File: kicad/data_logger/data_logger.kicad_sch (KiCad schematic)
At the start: 14 parts, among them M2 Motor_DC, M3 Motor_DC, M4 Motor_DC, U1 ARDUINO_MKR_WAN_1310

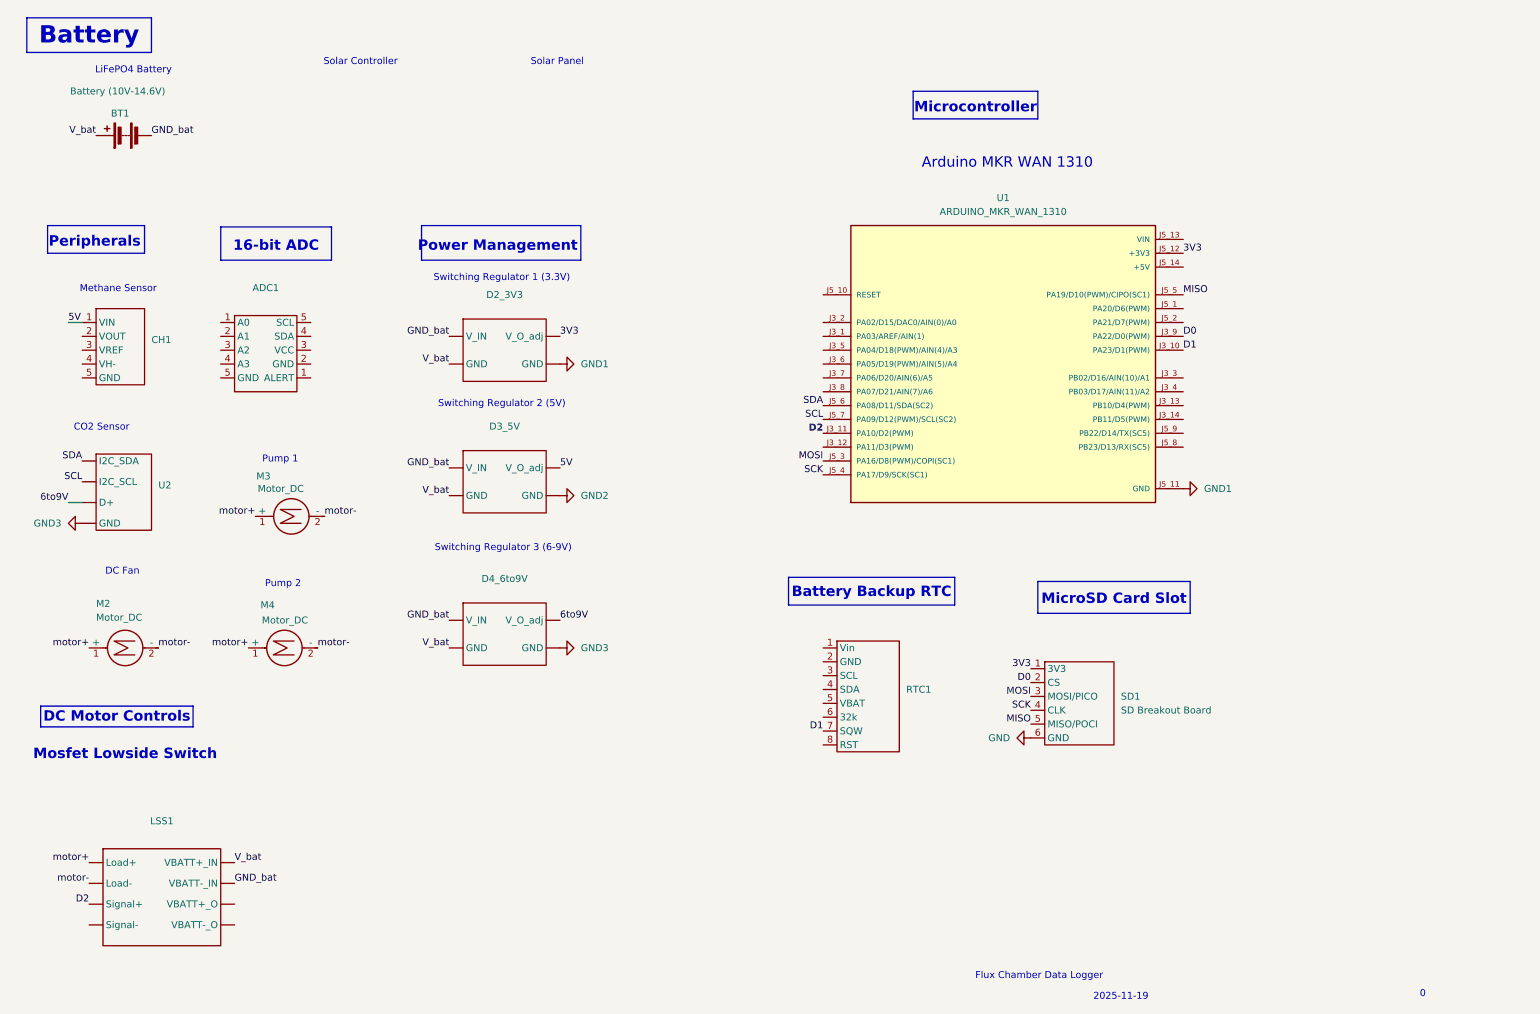
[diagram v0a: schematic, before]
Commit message: Updating schematics as I resolder things to the prototype
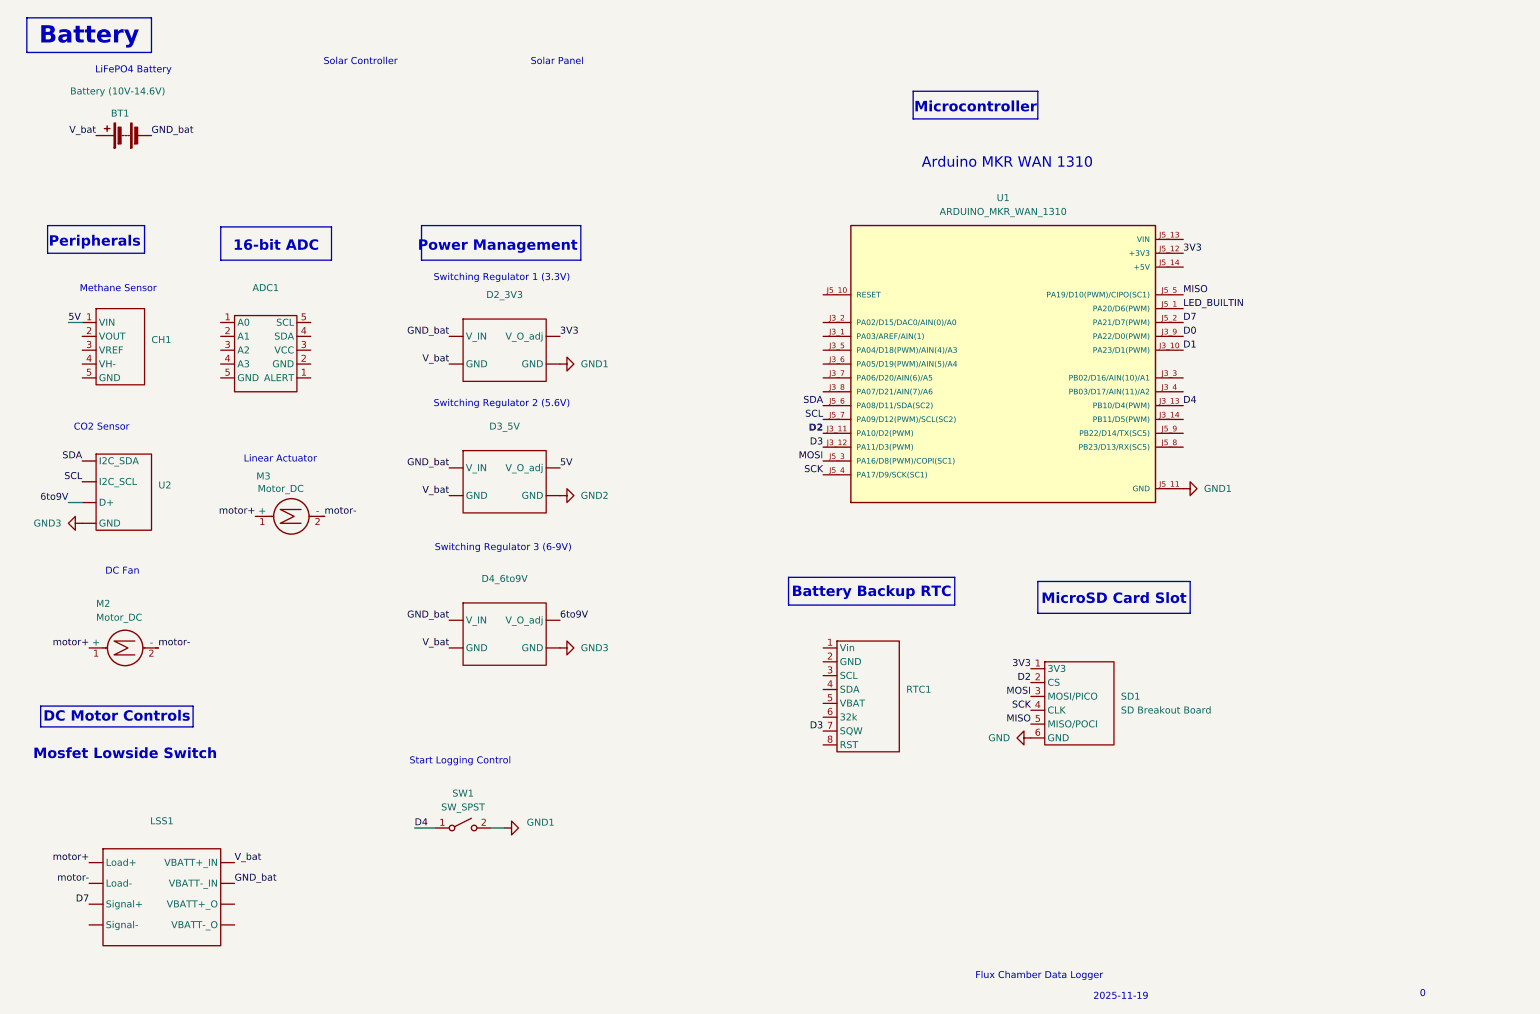
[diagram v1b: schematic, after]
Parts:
- removed M4: Motor_DC, symbol Motor:Motor_DC
- added SW1: SW_SPST, symbol Switch:SW_SPST
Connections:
- net D0: no longer SD1.2 (CS)
- net D1: no longer RTC1.7 (SQW)
- net D2: now also SD1.2 (CS); no longer LSS1. (VBATT-_O)
- net GND1: now also SW1.2 (B)
- net D3: now reaches U1.J3_12 (PA11/D3(PWM))
- net D3: now also RTC1.7 (SQW)
- net D4: now reaches U1.J3_13 (PB10/D4(PWM))
- net D4: now also SW1.1 (A)
- net LED_BUILTIN: now reaches U1.J5_1 (PA20/D6(PWM))
- net D7: now reaches U1.J5_2 (PA21/D7(PWM))
- net D7: now also LSS1. (VBATT-_O)
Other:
- note added: "Linear Actuator"
- note added: "Start Logging Control"
- note added: "Switching Regulator 2 (5.6V)"
- note removed: "Pump 1"
- note removed: "Pump 2"
- note removed: "Switching Regulator 2 (5V)"
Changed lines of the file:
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@@
 		)
 	)
-	(text "Pump 1"
+	(text "Linear Actuator\n"
 		(exclude_from_sim no)
 		(at 60.452 94.996 0)
@@
 		)
 	)
-	(text "Switching Regulator 2 (5V)\n"
+	(text "Switching Regulator 2 (5.6V)\n"
 		(exclude_from_sim no)
 		(at 101.092 84.836 0)
@@
 		)
 	)
-	(text "Pump 2"
-		(exclude_from_sim no)
-		(at 60.96 117.856 0)
+	(text "Start Logging Control"
+		(exclude_from_sim no)
+		(at 93.472 150.368 0)
 		(effects
 			(font
@@
 	(wire
 		(pts
-			(xy 21.59 69.85) (xy 24.13 69.85)
+			(xy 88.9 162.56) (xy 85.09 162.56)
 		)
 		(stroke
@@
 		)
 	)
+	(wire
+		(pts
+			(xy 21.59 69.85) (xy 24.13 69.85)
+		)
+		(stroke
+			(width 0)
+			(type default)
+		)
+	)
+	(wire
+		(pts
+			(xy 101.6 162.56) (xy 99.06 162.56)
+		)
+		(stroke
+			(width 0)
+			(type default)
+		)
+	)
 	(label "V_bat"
 		(at 52.07 168.91 0)
@@
 		)
 	)
-	(label "motor+"
-		(at 54.61 129.54 180)
-		(effects
-			(font
-				(size 1.27 1.27)
-			)
-			(justify right bottom)
-		)
-	)
 	(label "SDA"
 		(at 24.13 95.25 180)
@@
 		)
 	)
+	(label "D7"
+		(at 25.4 176.53 180)
+		(effects
+			(font
+				(size 1.27 1.27)
+			)
+			(justify right bottom)
+		)
+	)
 	(label "MISO"
 		(at 226.06 64.77 0)
@@
 		)
 	)
-	(label "D2"
-		(at 25.4 176.53 180)
-		(effects
-			(font
-				(size 1.27 1.27)
-			)
-			(justify right bottom)
+	(label "D4"
+		(at 226.06 85.09 0)
+		(effects
+			(font
+				(size 1.27 1.27)
+			)
+			(justify left bottom)
 		)
 	)
@@
 		)
 	)
-	(label "motor-"
-		(at 67.31 129.54 0)
-		(effects
-			(font
-				(size 1.27 1.27)
-			)
-			(justify left bottom)
-		)
-	)
 	(label "SCL"
 		(at 24.13 99.06 180)
@@
 		)
 	)
+	(label "LED_BUILTIN"
+		(at 226.06 67.31 0)
+		(effects
+			(font
+				(size 1.27 1.27)
+			)
+			(justify left bottom)
+		)
+	)
 	(label "V_bat"
 		(at 91.44 101.6 180)
@@
 		)
 	)
-	(label "D0"
+	(label "D7"
+		(at 226.06 69.85 0)
+		(effects
+			(font
+				(size 1.27 1.27)
+			)
+			(justify left bottom)
+		)
+	)
+	(label "D2"
 		(at 198.12 135.89 180)
 		(effects
@@
 		)
 	)
-	(label "D1"
+	(label "D3"
 		(at 160.02 144.78 180)
 		(effects
@@
 		)
 	)
+	(label "D4"
+		(at 85.09 162.56 0)
+		(effects
+			(font
+				(size 1.27 1.27)
+			)
+			(justify left bottom)
+		)
+	)
 	(label "V_bat"
 		(at 91.44 77.47 180)
@@
 	(label "GND_bat"
 		(at 91.44 96.52 180)
+		(effects
+			(font
+				(size 1.27 1.27)
+			)
+			(justify right bottom)
+		)
+	)
+	(label "D3"
+		(at 160.02 92.71 180)
 		(effects
 			(font
@@
 	)
 	(symbol
+		(lib_id "Switch:SW_SPST")
+		(at 93.98 162.56 0)
+		(unit 1)
+		(exclude_from_sim no)
+		(in_bom yes)
+		(on_board yes)
+		(dnp no)
+		(fields_autoplaced yes)
+		(property "Reference" "SW1"
+			(at 93.98 156.21 0)
+			(effects
+				(font
+					(size 1.27 1.27)
+				)
+			)
+		)
+		(property "Value" "SW_SPST"
+			(at 93.98 158.75 0)
+			(effects
+				(font
+					(size 1.27 1.27)
+				)
+			)
+		)
+		(property "Footprint" ""
+			(at 93.98 162.56 0)
+			(effects
+				(font
+					(size 1.27 1.27)
+				)
+				(hide yes)
+			)
+		)
+		(property "Datasheet" "~"
+			(at 93.98 162.56 0)
+			(effects
+				(font
+					(size 1.27 1.27)
+				)
+				(hide yes)
+			)
+		)
+		(property "Description" "Single Pole Single Throw (SPST) switch"
+			(at 93.98 162.56 0)
+			(effects
+				(font
+					(size 1.27 1.27)
+				)
+				(hide yes)
+			)
+		)
+		(pin "2"
+		)
+		(pin "1"
+		)
+		(instances
+			(project ""
+				(path "/6e8062db-1165-40d3-b0a8-95f723efc855"
+					(reference "SW1")
+					(unit 1)
+				)
+			)
+		)
+	)
+	(symbol
 		(lib_id "Device:Battery")
 		(at 31.75 35.56 90)
@@
 	)
 	(symbol
-		(lib_id "Motor:Motor_DC")
-		(at 59.69 129.54 90)
-		(unit 1)
-		(exclude_from_sim no)
-		(in_bom yes)
-		(on_board yes)
-		(dnp no)
-		(property "Reference" "M4"
-			(at 59.436 121.666 90)
-			(effects
-				(font
-					(size 1.27 1.27)
-				)
-				(justify left)
-			)
-		)
-		(property "Value" "Motor_DC"
-			(at 65.532 124.46 90)
-			(effects
-				(font
-					(size 1.27 1.27)
-				)
-				(justify left)
-			)
-		)
-		(property "Footprint" ""
-			(at 61.976 129.54 0)
-			(effects
-				(font
-					(size 1.27 1.27)
-				)
-				(hide yes)
-			)
-		)
-		(property "Datasheet" "~"
-			(at 61.976 129.54 0)
-			(effects
-				(font
-					(size 1.27 1.27)
-				)
-				(hide yes)
-			)
-		)
-		(property "Description" "DC Motor"
-			(at 59.69 129.54 0)
-			(effects
-				(font
-					(size 1.27 1.27)
-				)
-				(hide yes)
-			)
-		)
-		(pin "1"
-		)
-		(pin "2"
-		)
-		(instances
-			(project ""
-				(path "/6e8062db-1165-40d3-b0a8-95f723efc855"
-					(reference "M4")
-					(unit 1)
-				)
-			)
-		)
-	)
-	(symbol
 		(lib_id "power:GND")
 		(at 198.12 146.05 270)
@@
 					(unit 1)
 				)
+			)
+		)
+	)
+	(symbol
+		(lib_id "power:GND1")
+		(at 101.6 162.56 90)
+		(unit 1)
+		(exclude_from_sim no)
+		(in_bom yes)
+		(on_board yes)
+		(dnp no)
+		(property "Reference" "#PWR07"
+			(at 107.95 162.56 0)
+			(effects
+				(font
+					(size 1.27 1.27)
+				)
+				(hide yes)
+			)
+		)
+		(property "Value" "GND1"
+			(at 108.204 161.544 90)
+			(effects
+				(font
+					(size 1.27 1.27)
+				)
+			)
+		)
+		(property "Footprint" ""
+			(at 101.6 162.56 0)
+			(effects
+				(font
+					(size 1.27 1.27)
+				)
+				(hide yes)
+			)
+		)
+		(property "Datasheet" ""
+			(at 101.6 162.56 0)
+			(effects
+				(font
+					(size 1.27 1.27)
+				)
+				(hide yes)
+			)
+		)
+		(property "Description" "Power symbol creates a global label with name \"GND1\" , ground"
+			(at 101.6 162.56 0)
+			(effects
+				(font
+					(size 1.27 1.27)
+				)
+				(hide yes)
+			)
+		)
+		(pin "1"
+		)
+		(instances
+			(project ""
+				(path "/6e8062db-1165-40d3-b0a8-95f723efc855"
+					(reference "#PWR07")
+					(unit 1)
+				)

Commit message: Adding INA228 chip to schematics and cleaning things up a bit
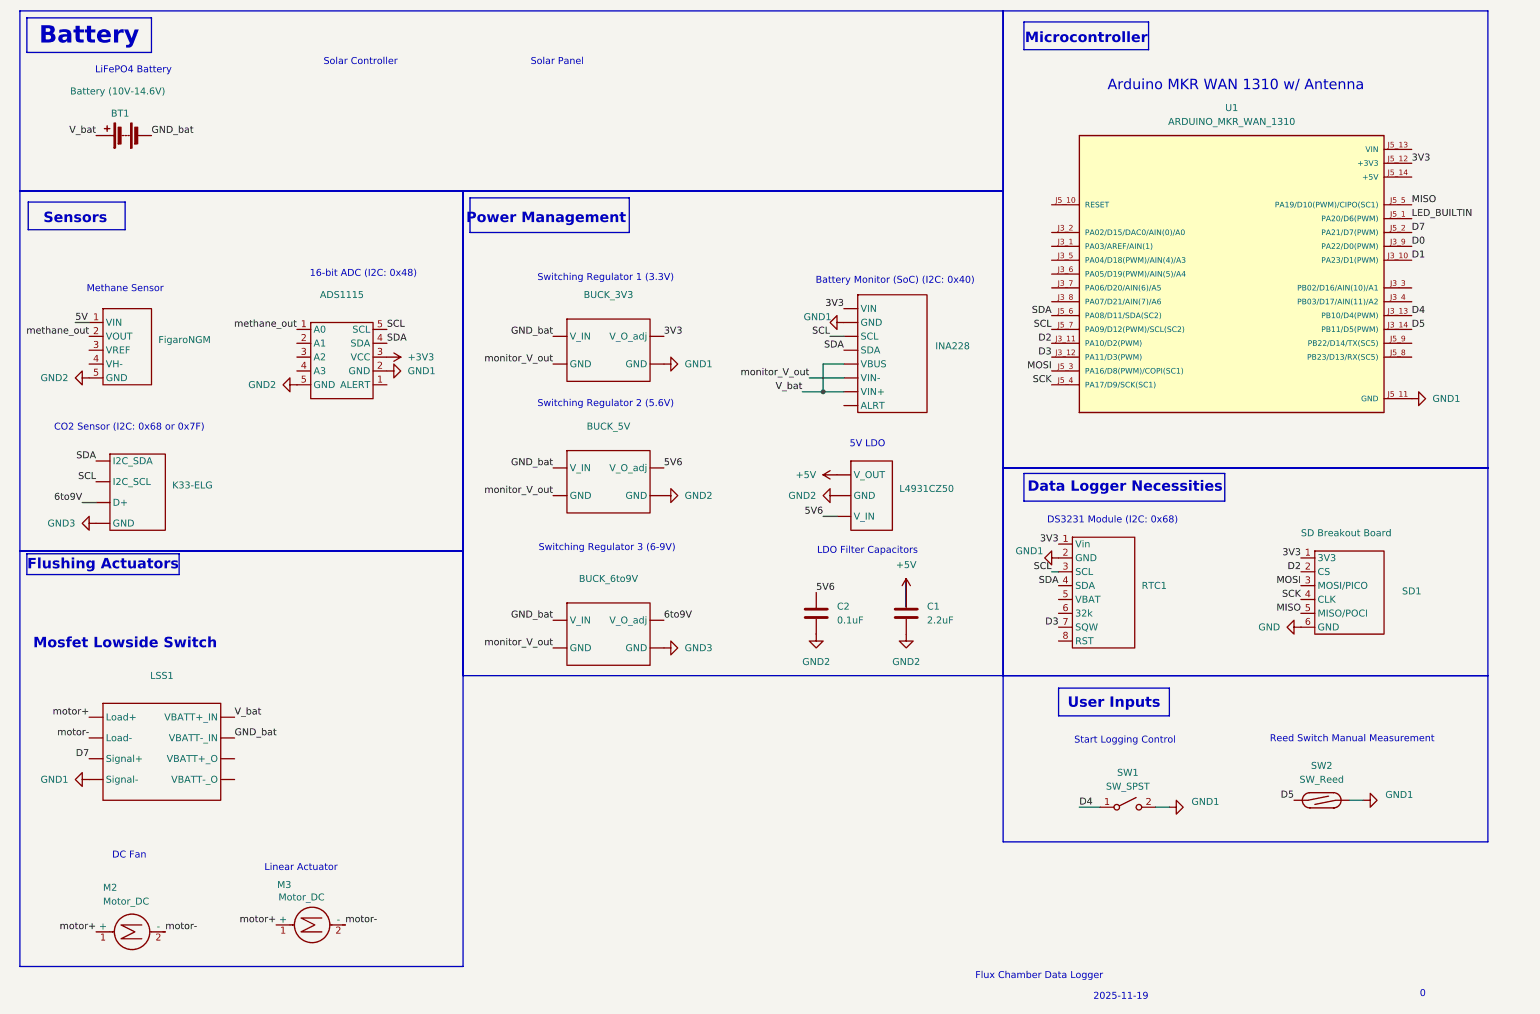
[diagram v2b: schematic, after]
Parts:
- added C1: 2.2uF, symbol Device:C
- added C2: 0.1uF, symbol Device:C
- added INA228: ~, symbol new_library:adafruit_ina228
- added L4931CZ50: ~, symbol new_library:5V_LDO_L4931CZ50
- added SW2: SW_Reed, symbol Switch:SW_Reed
- renumbered ADC1 to ADS1115, D2_3V3 to BUCK_3V3, D3_5V to BUCK_5V, D4_6to9V to BUCK_6to9V, CH1 to FigaroNGM, U2 to K33-ELG
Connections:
- net 3V3: now also RTC1.1 (Vin), INA228. (ALRT)
- net 5V: no longer BUCK_5V. (GND)
- net GND1: now also ADS1115.2 (GND), LSS1. (VBATT-_O), RTC1.2 (GND), INA228. (ALRT), SW2.2
- net GND2: now also ADS1115.5 (SCL), FigaroNGM.5 (GND), C1.2, C2.2, L4931CZ50. (V_IN)
- net SCL: now also ADS1115.5 (SCL), RTC1.3 (SCL), INA228. (ALRT)
- net SDA: now also ADS1115.4 (SDA), RTC1.4 (SDA), INA228. (ALRT)
- net V_bat: now also INA228. (ALRT); no longer BUCK_3V3. (GND), BUCK_5V. (GND), BUCK_6to9V. (GND)
- net methane_out: now reaches FigaroNGM.2 (VOUT)
- net methane_out: now also ADS1115.1 (ALERT)
- net D5: now reaches U1.J3_14 (PB11/D5(PWM))
- net D5: now also SW2.1
- net +3V3: now reaches ADS1115.3 (VCC)
- new net +5V: C1.1, L4931CZ50. (V_IN)
- new net 5V6: BUCK_5V. (GND), C2.1, L4931CZ50. (V_IN)
- new net monitor_V_out: BUCK_3V3. (GND), BUCK_5V. (GND), BUCK_6to9V. (GND), INA228. (ALRT)
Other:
- note added: "16-bit ADC (I2C: 0x48)"
- note added: "5V LDO"
- note added: "Arduino MKR WAN 1310 w/ Antenna"
- note added: "Battery Monitor (SoC) (I2C: 0x40)"
- note added: "CO2 Sensor (I2C: 0x68 or 0x7F)"
- note added: "DS3231 Module (I2C: 0x68)"
- note added: "Data Logger Necessities"
- note added: "Flushing Actuators"
- note added: "LDO Filter Capacitors"
- note added: "Reed Switch Manual Measurement"
- note added: "Sensors"
- note added: "User Inputs"
- note removed: "16-bit ADC"
- note removed: "Arduino MKR WAN 1310"
- note removed: "Battery Backup RTC"
- note removed: "CO2 Sensor"
- note removed: "DC Motor Controls"
- note removed: "MicroSD Card Slot"
- note removed: "Peripherals"
- moved on the sheet: ADS1115, BUCK_3V3, BUCK_5V, BUCK_6to9V, FigaroNGM, K33-ELG, LSS1, M2, M3, RTC1, SD1, SW1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

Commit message: Making more changes. Thinking of still using the connectors to deliver various power levels
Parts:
- removed U1: ARDUINO_MKR_WAN_1310, ARDUINO_MKR_WAN_1310:BOARD_ARDUINO_MKR_WAN_1310, symbol new_library:ARDUINO_MKR_WAN_1310
- added A1: Arduino_MKR_WAN_1310_Socket, PCM_arduino-library:Arduino_MKR_FOX_1200_Socket, symbol PCM_arduino-library:Arduino_MKR_WAN_1310_Socket
- added M4: Motor_Servo, symbol Motor:Motor_Servo
- renumbered BUCK_5V to BUCK_5V1, BUCK_6to9V to BUCK_6to9V1, FigaroNGM to FigaroNGM1, K33-ELG to K33-ELG1
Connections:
- net +3V3 is gone; now on net 3V3: ADS1115.3 (VCC)
- net 3V3: now also A1.3V3 (3.3V)
- net 6to9V: now also M4.2 (+)
- net D2: now also A1.D2
- net D3: now also A1.D3
- net D4: now also A1.D4
- net D5: now also A1.D5
- net D7: now also A1.D7
- net GND1: now also A1.GND
- net GND3: now also M4.3 (-)
- net LED_BUILTIN: now also A1.D6
- net MISO: now also A1.D10 (D10_MISO)
- net MOSI: now also A1.D8 (D8_MOSI)
- net SCK: now also A1.D9 (D9_SCK)
- net SCL: now also A1.D12 (D12/SCL)
- net SDA: now also A1.D11 (D11/SDA)
- new net PWM_motor: A1.D1, M4.1 (PWM)
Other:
- note added: "Bucket Tilt Servo"
